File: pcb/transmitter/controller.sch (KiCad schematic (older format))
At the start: 43 parts, among them J1 Conn_01x01, J2 Conn_01x02, J3 Conn_01x03, J4 Conn_02x02_Odd_Even, Q1 RU1C001ZPTL, Q2 CSD25481F4T, Q3 BC847BLT1G, U1 TPS613222ADBVR, U2 LIS2DE12TR, U3 MSP430FR2512IRHLR, U4 BMG250, Y1 32.786kHz

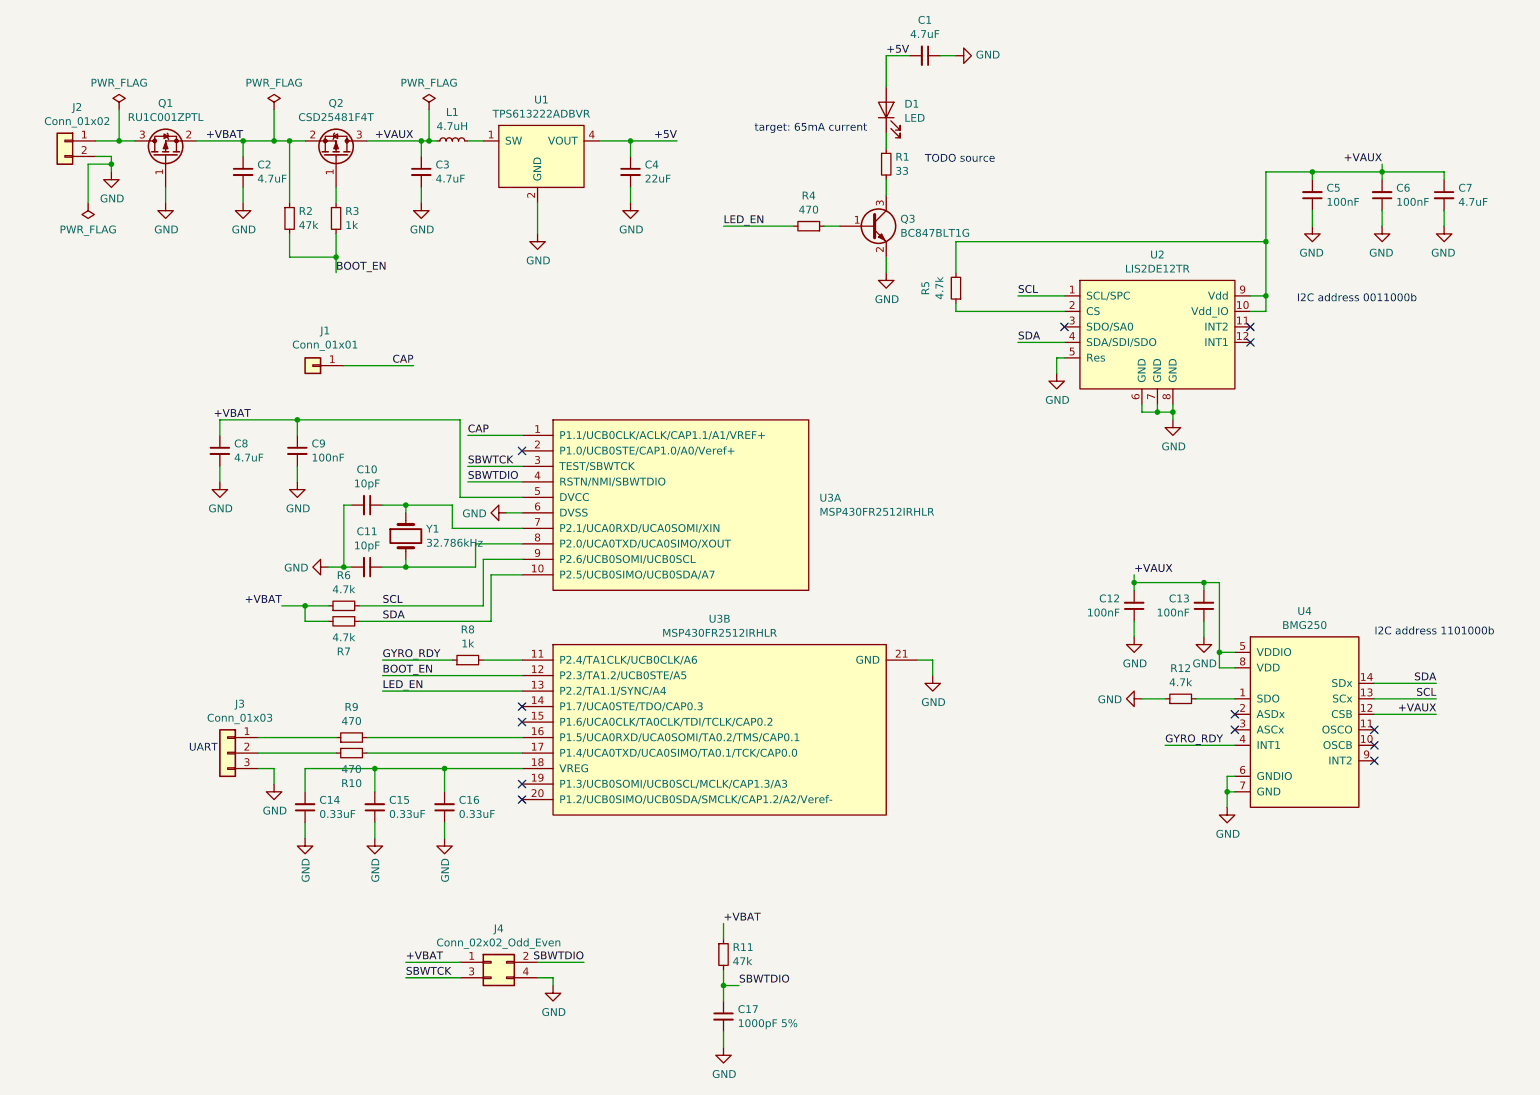
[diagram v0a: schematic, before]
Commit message: (Rev 2) Finish relayout; add load switch and upgrade protection FET, add filter resistors to digital power rails TODO fix up silkscreen
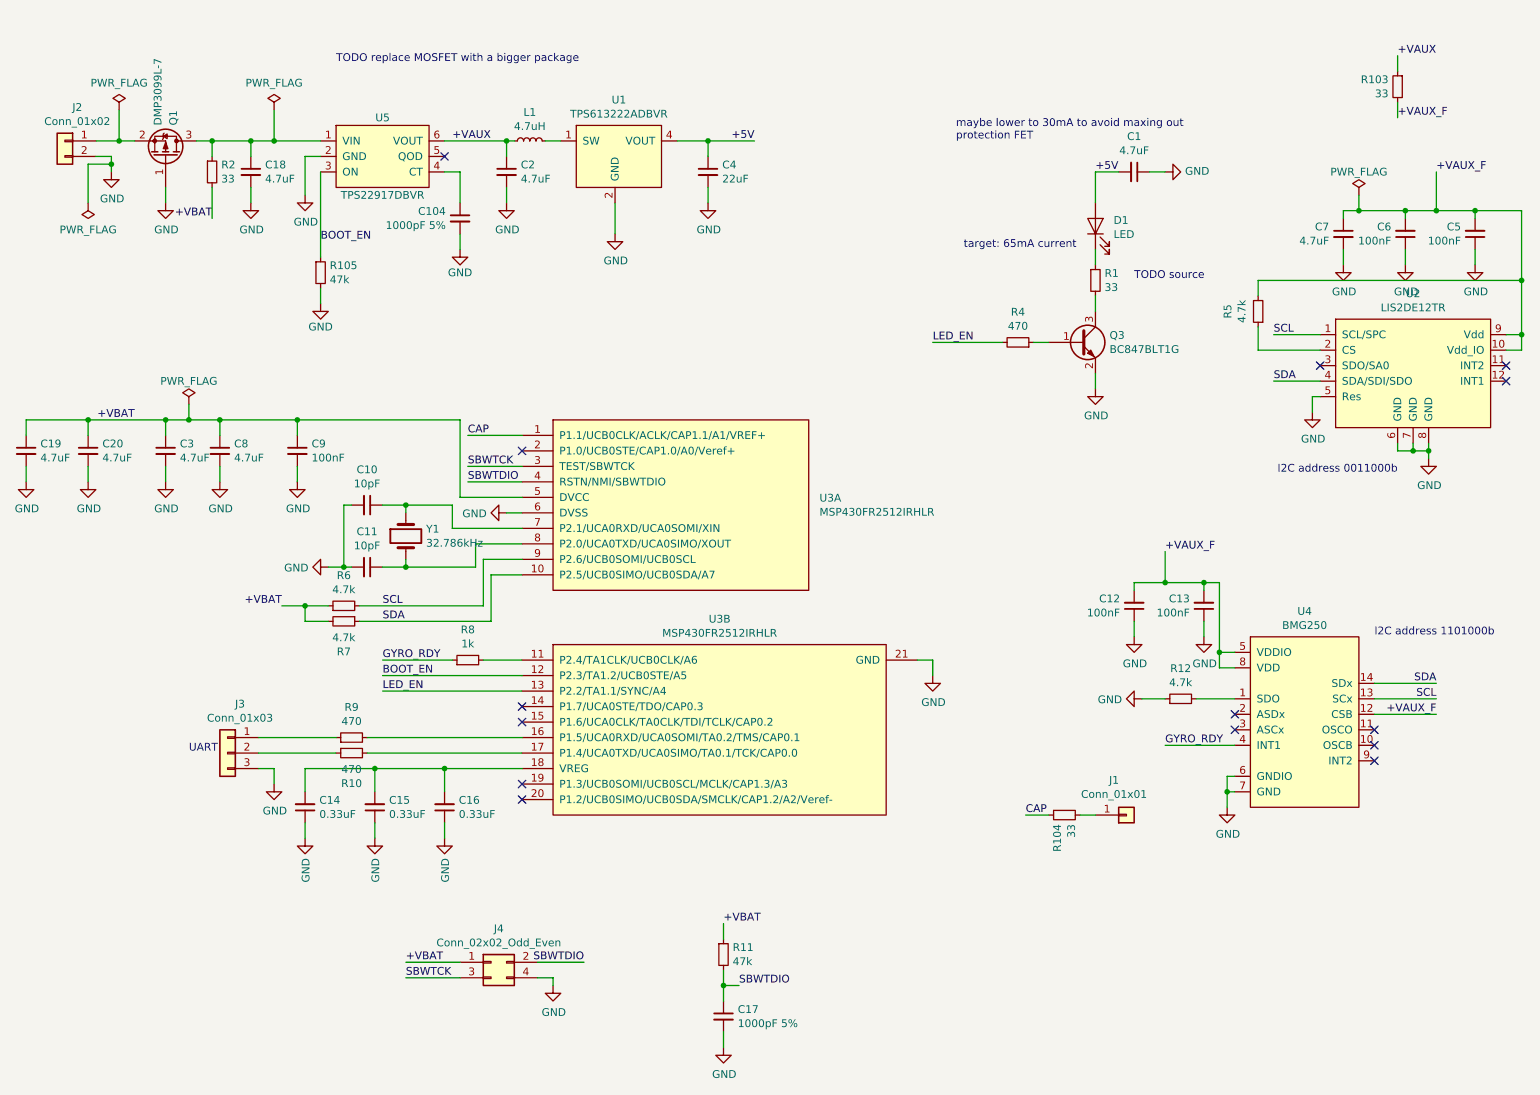
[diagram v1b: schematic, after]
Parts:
- removed Q2: CSD25481F4T, controller:TI_Femto0402, symbol Device:Q_PMOS_GSD
- removed R3: 1k, Resistors_SMD:R_0603_HandSoldering, symbol Device:R_Small
- added C104: 1000pF 5%, Capacitors_SMD:C_0805_HandSoldering, symbol Device:C_Small
- added C18, C19, C20: 4.7uF, Capacitors_SMD:C_0603_HandSoldering, symbol Device:C_Small
- added R103, R104: 33, Resistors_SMD:R_0603_HandSoldering, symbol Device:R_Small
- added R105: 47k, Resistors_SMD:R_0603_HandSoldering, symbol Device:R_Small
- added U5: TPS22917DBVR, TO_SOT_Packages_SMD:SOT-23-6_Handsoldering, symbol controllerparts:TPS22917DBVR
- Q1: value RU1C001ZPTL -> DMP3099L-7; footprint controller:Rohm_UMT3F -> TO_SOT_Packages_SMD:SOT-23_Handsoldering; Mouser 755-RU1C001ZPTL -> 621-DMP3099L-7
- R2: value 47k -> 33; Mouser 603-RC0603JR-0747KL -> (none)
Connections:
- net +VAUX: now also C2.1, R103.1, U5.6 (VOUT); no longer C12.2, C13.2, C3.1, C5.2, C6.2, C7.1, R5.2, U2.10 (Vdd_IO), U2.9 (Vdd), U4.12 (CSB), U4.5 (VDDIO), U4.8 (VDD)
- net +VBAT: now also C3.1, R2.2, C19.1, C20.1; no longer C2.1, Q1.2 (S), R2.1
- net BOOT_EN: now also R105.1, U5.3 (ON); no longer R2.2
- net CAP: now also R104.1; no longer J1.1 (Pin_1)
- net GND: now also C104.2, C18.2, C19.2, C20.2, R105.2, U5.2 (GND)
- net at J2.1 (Pin_1): now also Q1.2 (S); no longer Q1.3 (D)
- new net: J1.1 (Pin_1), R104.2
- new net: C18.1, Q1.3 (D), R2.1, U5.1 (VIN)
- new net: C104.1, U5.4 (CT)
- new net +VAUX_F: C12.2, C13.2, C5.2, C6.2, C7.1, R103.2, R5.2, U2.10 (Vdd_IO), U2.9 (Vdd), U4.12 (CSB), U4.5 (VDDIO), U4.8 (VDD)
- no-connect marks 13 -> 14
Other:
- note added: "TODO replace MOSFET with a bigger package"
- note added: "maybe lower to 30mA to avoid maxing out \nprotection FET"
- moved on the sheet: C1, C2, C3, C4, C5, C6, C7, D1, J1, L1, Q3, R1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

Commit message: Finish silkscreen layout
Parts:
- R1: Mouser (none) -> 755-ESR03EZPJ330
- renumbered C104 to C21, R104 to R13, R103 to R14, R105 to R3
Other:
- note removed: "TODO replace MOSFET with a bigger package"
- note removed: "TODO source"
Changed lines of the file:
@@
 F 2 "Resistors_SMD:R_0603_HandSoldering" H 7500 2550 50  0001 C CNN
 F 3 "~" H 7500 2550 50  0001 C CNN
+F 4 "755-ESR03EZPJ330" H 7500 2550 50  0001 C CNN "Mouser"
 	1    7500 2550
 	1    0    0    -1
@@
 	9650 3700 9650 3650
 Connection ~ 9650 3650
-Text Notes 7750 2550 0    50   ~ 0
-TODO source
 Text Notes 6600 1650 0    50   ~ 0
 maybe lower to 30mA to avoid maxing out \nprotection FET
@@
 Wire Wire Line
 	1000 3550 1000 3450
-Text Notes 2600 1150 0    50   ~ 0
-TODO replace MOSFET with a bigger package
 $Comp
 L Device:C_Small C19
@@
 	2050 1950 2050 2050
 $Comp
-L Device:R_Small R103
+L Device:R_Small R14
 U 1 1 5C0D2F74
 P 9450 1300
-F 0 "R103" H 9509 1346 50  0000 L CNN
+F 0 "R14" H 9509 1346 50  0000 L CNN
 F 1 "33" H 9509 1255 50  0000 L CNN
 F 2 "Resistors_SMD:R_0603_HandSoldering" H 9450 1300 50  0001 C CNN
@@
 	7950 4500 7750 4500
 $Comp
-L Device:R_Small R104
+L Device:R_Small R13
 U 1 1 5C0BE646
 P 7300 6000
-F 0 "R104" H 7359 6046 50  0000 L CNN
+F 0 "R13" H 7359 6046 50  0000 L CNN
 F 1 "33" H 7359 5955 50  0000 L CNN
 F 2 "Resistors_SMD:R_0603_HandSoldering" H 7300 6000 50  0001 C CNN
@@
 	3400 1850 3300 1850
 $Comp
-L Device:R_Small R105
+L Device:R_Small R3
 U 1 1 5C1B79B9
 P 2500 2500
-F 0 "R105" H 2559 2546 50  0000 L CNN
+F 0 "R3" H 2559 2546 50  0000 L CNN
 F 1 "47k" H 2559 2455 50  0000 L CNN
 F 2 "Resistors_SMD:R_0603_HandSoldering" H 2500 2500 50  0001 C CNN
@@
 	2500 2600 2500 2700
 $Comp
-L Device:C_Small C104
+L Device:C_Small C21
 U 1 1 5C1F11FD
 P 3400 2150
-F 0 "C104" H 3492 2196 50  0000 L CNN
+F 0 "C21" H 3492 2196 50  0000 L CNN
 F 1 "1000pF 5%" H 3492 2105 50  0000 L CNN
 F 2 "Capacitors_SMD:C_0805_HandSoldering" H 3400 2150 50  0001 C CNN

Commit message: I guess I modified some of the schematics somewhere?
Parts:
- R13, R14, R2: Mouser (none) -> 755-ESR03EZPJ330
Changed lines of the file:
@@
 F 2 "Resistors_SMD:R_0603_HandSoldering" H 1800 1850 50  0001 C CNN
 F 3 "~" H 1800 1850 50  0001 C CNN
+F 4 "755-ESR03EZPJ330" H 1800 1850 50  0001 C CNN "Mouser"
 	1    1800 1850
 	1    0    0    -1
@@
 F 2 "Resistors_SMD:R_0603_HandSoldering" H 9450 1300 50  0001 C CNN
 F 3 "~" H 9450 1300 50  0001 C CNN
+F 4 "755-ESR03EZPJ330" H 9450 1300 50  0001 C CNN "Mouser"
 	1    9450 1300
 	-1   0    0    -1
@@
 F 2 "Resistors_SMD:R_0603_HandSoldering" H 7300 6000 50  0001 C CNN
 F 3 "~" H 7300 6000 50  0001 C CNN
+F 4 "755-ESR03EZPJ330" H 7300 6000 50  0001 C CNN "Mouser"
 	1    7300 6000
 	0    -1   1    0
